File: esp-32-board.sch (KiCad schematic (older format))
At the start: 12 parts, among them J2 Conn_Arduino_UNO_R3, J3 Conn_02x03_Odd_Even, J4 ESP-PROG-Program, J5 ESP-PROG-Debug, SW1 SW_Push, SW2 SW_Push, U3 ESP32-WROOM-32

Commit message: Reorganize symbols & update vendors
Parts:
- C1: renamed from C3; value C -> 4.7uF; Vendor (none) -> avt.pl; VendorLink (none) -> https://sklep.avt.pl/zestaw-kondensatorow-smd-0805-720-sztu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
- C2: renamed from C4; value C -> 100nF; Vendor (none) -> avt.pl; VendorLink (none) -> https://sklep.avt.pl/zestaw-kondensatorow-smd-0805-720-sztu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
- C3: renamed from C5; value C -> 100nF; Vendor (none) -> avt.pl; VendorLink (none) -> https://sklep.avt.pl/zestaw-kondensatorow-smd-0805-720-sztu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
- C4: renamed from C6; value C -> 100nF; Vendor (none) -> avt.pl; VendorLink (none) -> https://sklep.avt.pl/zestaw-kondensatorow-smd-0805-720-sztu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
- J1: renamed from J2; Vendor (none) -> N/A
- J2: renamed from J3; Vendor (none) -> N/A
- RN1: Vendor (none) -> tme.eu; VendorLink (none) -> https://www.tme.eu/pl/en/details/dr0804-100r-4_8/smd-resist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
- renumbered J4 to J3, J5 to J4, SW2 to SW1, SW1 to SW2, U3 to U1

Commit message: Remove Op-Amp circuit for USB power
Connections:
- net labels removed: VBUS
- wire segments 138 -> 137
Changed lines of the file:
@@
 F2 "VIN" U R 4300 6550 50
 F3 "+5V" U R 4300 6700 50
-F4 "VBUS" U L 3250 6600 50
 F5 "+3.3V" U R 4300 6850 50
 F6 "Internal_3V3" U R 4300 7050 50
@@
 F0 "USB" 50
 F1 "usb.sch" 50
-F2 "VBUS" O R 2200 6600 50
-F3 "EN" O R 2200 6800 50
-F4 "IO0" O R 2200 6950 50
-F5 "TXD0" I L 1150 6600 50
-F6 "RXD0" O L 1150 6750 50
-F7 "Internal_3V3" U L 1150 7050 50
+F2 "EN" O R 2200 6800 50
+F3 "IO0" O R 2200 6950 50
+F4 "TXD0" I L 1150 6600 50
+F5 "RXD0" O L 1150 6750 50
+F6 "Internal_3V3" U L 1150 7050 50
+F7 "+5V" U R 2200 6550 50
 $EndSheet
 Text Label 2500 6950 2    50   ~ 0
@@
 $EndComp
 $Comp
-L power:VBUS #PWR06
-U 1 1 5FC51FB0
-P 2800 6250
-F 0 "#PWR06" H 2800 6100 50  0001 C CNN
-F 1 "VBUS" H 2850 6450 50  0000 C CNN
-F 2 "" H 2800 6250 50  0001 C CNN
-F 3 "" H 2800 6250 50  0001 C CNN
-	1    2800 6250
-	1    0    0    -1
-$EndComp
-$Comp
 L power:VDC #PWR015
 U 1 1 5FD163B8
@@
 $EndComp
 Wire Wire Line
-	2800 6600 3250 6600
-Wire Wire Line
-	2200 6600 2800 6600
-Connection ~ 2800 6600
-Wire Wire Line
-	2800 6250 2800 6600
-Wire Wire Line
 	4300 7050 4450 7050
 Wire Wire Line
@@
 Wire Wire Line
 	1050 7050 1150 7050
+$Comp
+L power:+5V #PWR?
+U 1 1 5FB38759
+P 2350 6250
+F 0 "#PWR?" H 2350 6100 50  0001 C CNN
+F 1 "+5V" H 2400 6450 50  0000 C CNN
+F 2 "" H 2350 6250 50  0001 C CNN
+F 3 "" H 2350 6250 50  0001 C CNN
+	1    2350 6250
+	1    0    0    -1
+$EndComp
+Wire Wire Line
+	2200 6550 2350 6550
+Wire Wire Line
+	2350 6550 2350 6250
 $EndSCHEMATC

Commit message: Update power switch
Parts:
- SW1, SW2: footprint Button_Switch_SMD:SW_Push_1P1T_NO_6x6mm_H9.5mm -> Button_Switch_SMD:SW_Push_1P1T_NO_6x6mm_H4.3mm; Vendor (none) -> tme.eu; VendorLink (none) -> https://www.tme.eu/pl/details/tactm-64n-f/mikroprzelaczniki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
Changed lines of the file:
@@
 F 0 "SW2" H 2350 4900 50  0000 C CNN
 F 1 "SW_Push" H 2350 4800 50  0000 C CNN
-F 2 "Button_Switch_SMD:SW_Push_1P1T_NO_6x6mm_H9.5mm" H 2350 4850 50  0001 C CNN
+F 2 "Button_Switch_SMD:SW_Push_1P1T_NO_6x6mm_H4.3mm" H 2350 4850 50  0001 C CNN
 F 3 "~" H 2350 4850 50  0001 C CNN
+F 4 "tme.eu" H 2350 4650 50  0001 C CNN "Vendor"
+F 5 "https://www.tme.eu/pl/details/tactm-64n-f/mikroprzelaczniki-tact/ninigi/" H 2350 4650 50  0001 C CNN "VendorLink"
 	1    2350 4650
 	1    0    0    -1
@@
 F 0 "SW1" H 3500 5000 50  0000 C CNN
 F 1 "SW_Push" H 3500 4900 50  0000 C CNN
-F 2 "Button_Switch_SMD:SW_Push_1P1T_NO_6x6mm_H9.5mm" H 3500 4900 50  0001 C CNN
+F 2 "Button_Switch_SMD:SW_Push_1P1T_NO_6x6mm_H4.3mm" H 3500 4900 50  0001 C CNN
 F 3 "~" H 3500 4900 50  0001 C CNN
+F 4 "tme.eu" H 3500 4700 50  0001 C CNN "Vendor"
+F 5 "https://www.tme.eu/pl/details/tactm-64n-f/mikroprzelaczniki-tact/ninigi/" H 3500 4700 50  0001 C CNN "VendorLink"
 	1    3500 4700
 	1    0    0    -1

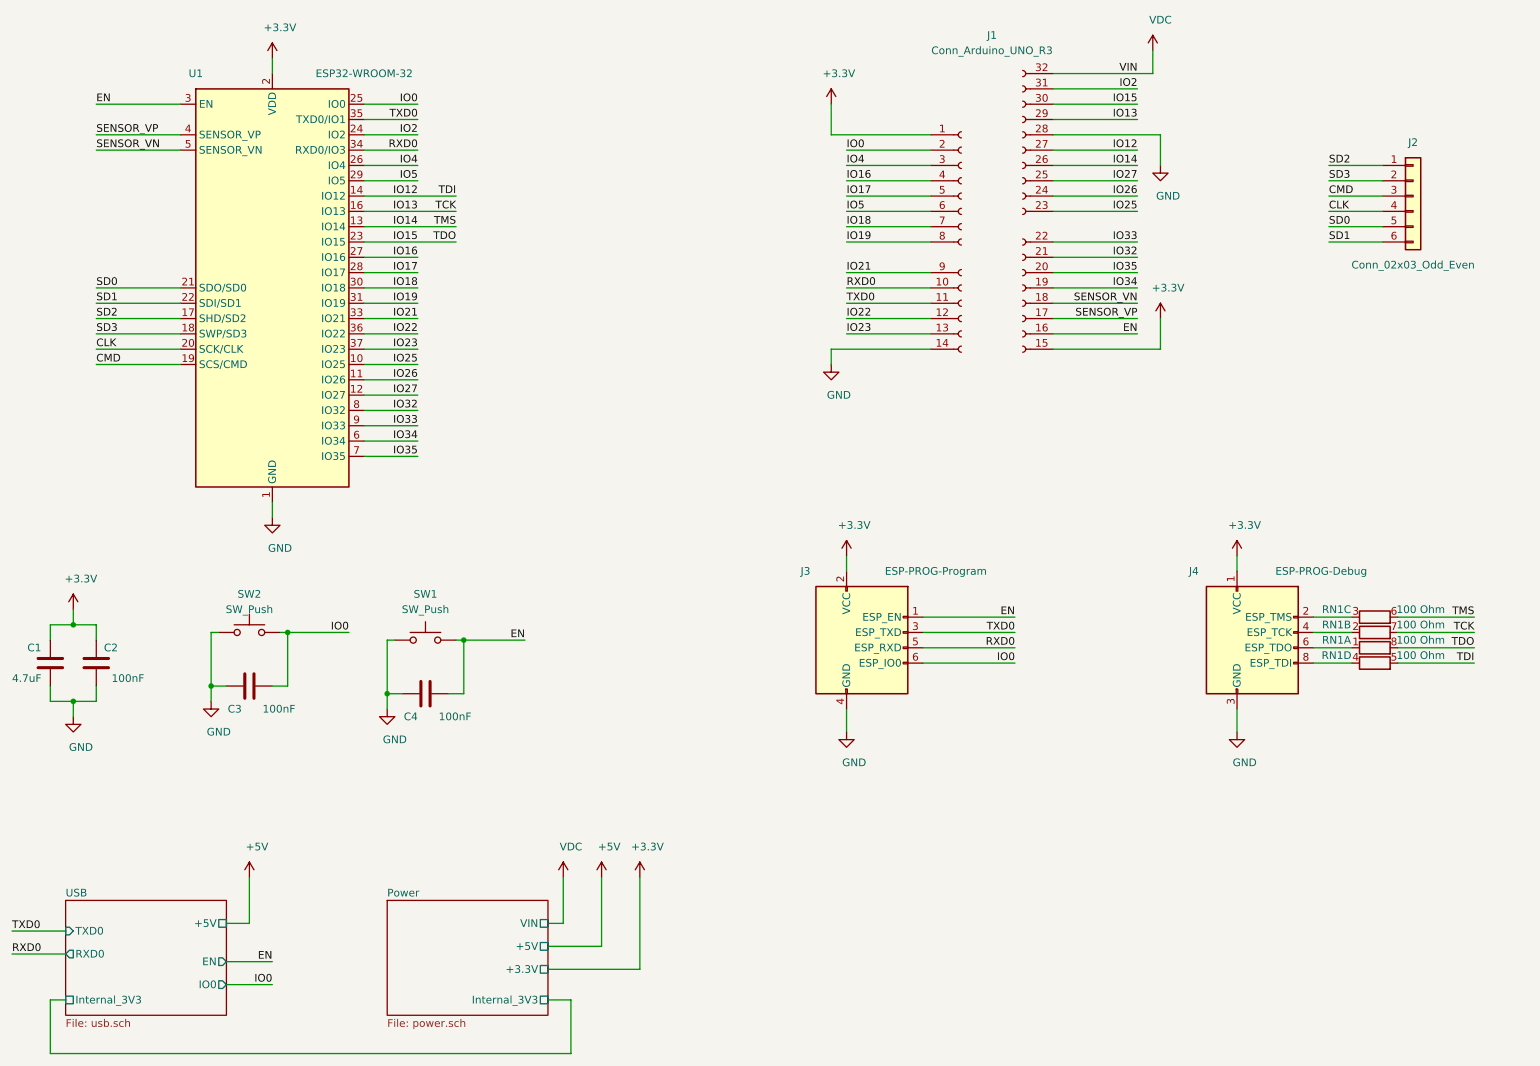
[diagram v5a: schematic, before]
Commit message: Schematic reorganization & reannotate
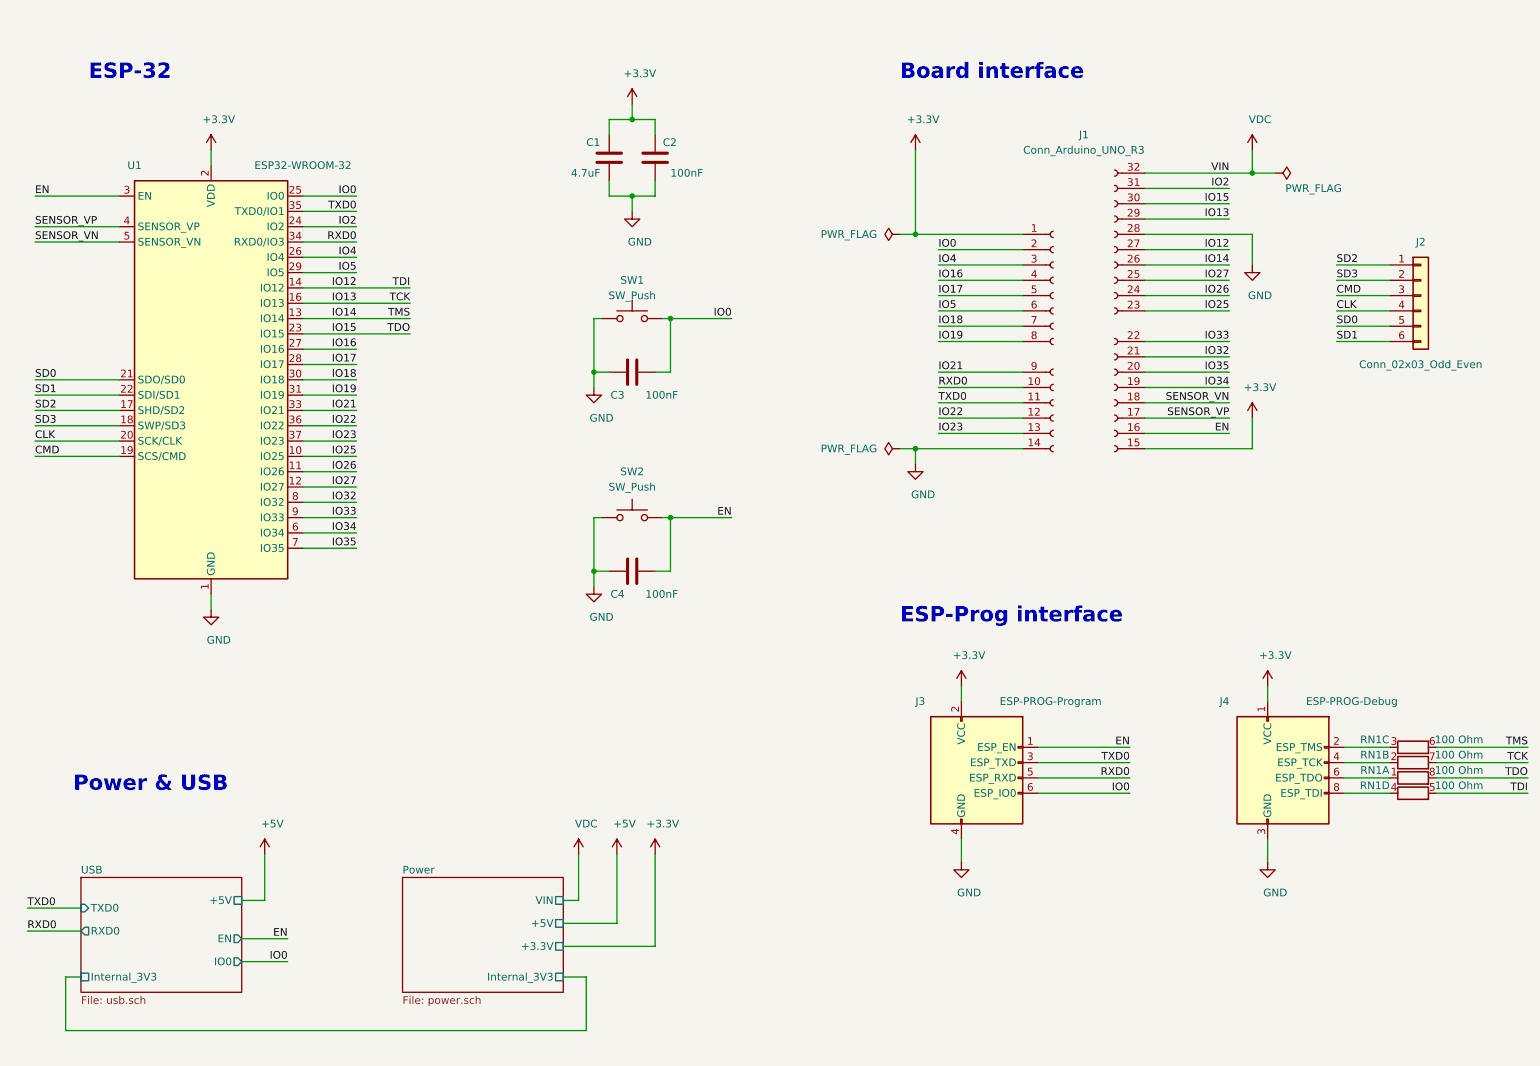
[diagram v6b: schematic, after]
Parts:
- renumbered SW2 to SW1, SW1 to SW2
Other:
- note added: "Board interface"
- note added: "ESP-32"
- note added: "ESP-Prog interface"
- note added: "Power & USB"
- moved on the sheet: C1, C2, C3, C4, J1, J2, J3, J4, RN1A, RN1B, RN1C, RN1D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
